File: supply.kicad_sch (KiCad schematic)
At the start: 39 parts, among them IC3 TPS259571DSGR, IC4 BQ27427YZFR, IC5 TPD6E001RSERG4, IC7 TPS62291DRVR, IC8 TPS62293DRVR, IC9 MP2722GRH-0000-Z, J4 UJ20-C-V-SMT-TR-68, J6 Conn_01x03

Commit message: cleaned up symbol fields table and removed unused or duplicate fields.
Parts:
- D1, D2: MFN (none) -> 755-SML-P12YTT86RR; MNR 755-SML-P12YTT86RR -> (none)
- IC3: MFN (none) -> 595-TPS259571DSGR; Manufacturer_Name Texas Instruments -> (none); Manufacturer_Part_Number TPS259571DSGR -> (none); Mouser Part Number 595-TPS259571DSGR -> (none); Mouser Price/Stock https://www.mouser.co.uk/ProductDetail/Texas-Instruments/TP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 -> (none)
- IC4: MFN (none) -> 595-BQ27427YZFR; Manufacturer_Name Texas Instruments -> (none); Manufacturer_Part_Number BQ27427YZFR -> (none); Mouser Part Number 595-BQ27427YZFR -> (none); Mouser Price/Stock https://www.mouser.co.uk/ProductDetail/Texas-Instruments/BQ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 -> (none)
- IC4: renamed from IC5; MFN (none) -> 595-TPD6E001RSERG4; Manufacturer_Name Texas Instruments -> (none); Manufacturer_Part_Number TPD6E001RSERG4 -> (none); Mouser Part Number 595-TPD6E001RSERG4 -> (none); Mouser Price/Stock https://www.mouser.co.uk/ProductDetail/Texas-Instruments/TP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 -> (none)
- IC5: renamed from IC9; MFN (none) -> 946-MP2722GRH-0000-Z; Manufacturer_Name Monolithic Power Systems (MPS) -> (none); Manufacturer_Part_Number MP2722GRH-0000-Z -> (none)
- IC6: renamed from IC7; MFN (none) -> 595-TPS62291DRVR; Manufacturer_Name Texas Instruments -> (none); Manufacturer_Part_Number TPS62291DRVR -> (none); Mouser Part Number 595-TPS62291DRVR -> (none); Mouser Price/Stock https://www.mouser.co.uk/ProductDetail/Texas-Instruments/TP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 -> (none)
- IC7: renamed from IC8; MFN (none) -> 595-TPS62293DRVR; Manufacturer_Name Texas Instruments -> (none); Manufacturer_Part_Number TPS62293DRVR -> (none); Mouser Part Number 595-TPS62293DRVR -> (none); Mouser Price/Stock https://www.mouser.co.uk/ProductDetail/Texas-Instruments/TP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 -> (none)
- J4: MFN (none) -> 179-UJ20-C-V-SMTTR68; Manufacturer_Name CUI Devices -> (none); Manufacturer_Part_Number UJ20-C-V-SMT-TR-68 -> (none); Mouser Part Number 179-UJ20-C-V-SMTTR68 -> (none); Mouser Price/Stock https://www.mouser.co.uk/ProductDetail/CUI-Devices/UJ20-C-V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 -> (none)
- renumbered C4 to C10, J6 to J5, L3 to L1, L1 to L2, L4 to L3, R16 to R10, R7 to R11, R10 to R12, R12 to R14, R18 to R15, R19 to R16, R8 to R7

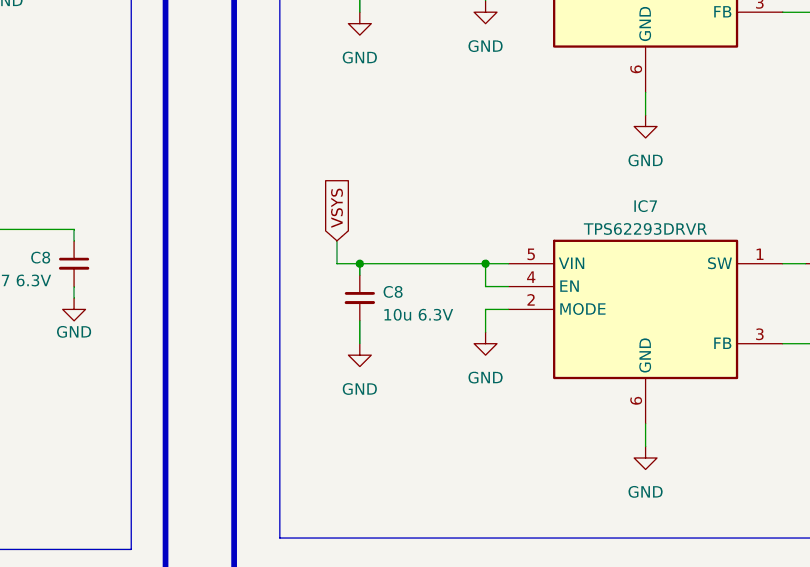
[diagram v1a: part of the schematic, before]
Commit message: switched to I2CB (so both M4 and A7 access), added 1v8 enable gpio and removed connection to vin
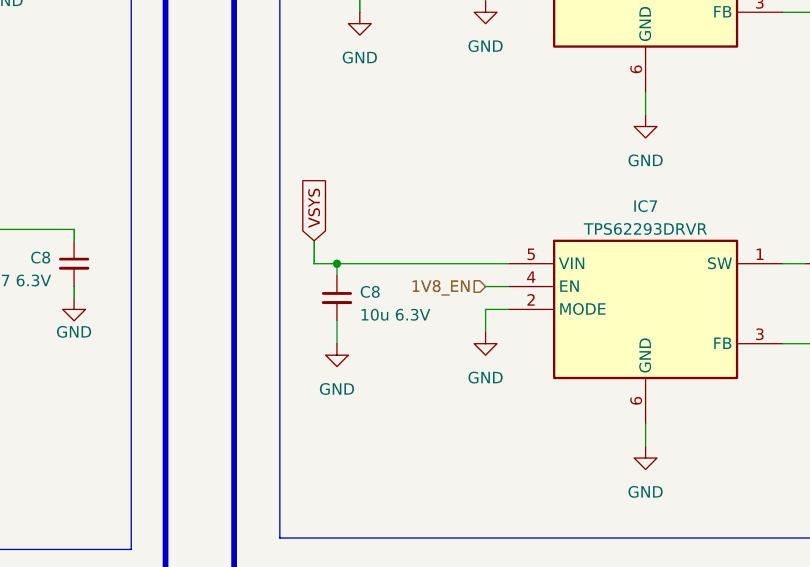
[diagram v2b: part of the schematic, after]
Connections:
- net VSYS: no longer IC7.4 (EN)
- new net 1V8_EN: IC7.4 (EN)
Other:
- moved on the sheet: C8
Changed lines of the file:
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@@
   (junction (at 254 134.62) (diameter 0) (color 0 0 0 0)
   )
-  (junction (at 330.2 176.53) (diameter 0) (color 0 0 0 0)
-  )
   (junction (at 240.03 45.72) (diameter 0) (color 0 0 0 0)
   )
@@
   (junction (at 238.76 134.62) (diameter 0) (color 0 0 0 0)
   )
-  (junction (at 316.23 176.53) (diameter 0) (color 0 0 0 0)
+  (junction (at 313.69 176.53) (diameter 0) (color 0 0 0 0)
   )
   (junction (at 261.62 134.62) (diameter 0) (color 0 0 0 0)
@@
     (stroke (width 0) (type default))
   )
-  (wire (pts (xy 316.23 182.88) (xy 316.23 185.42))
+  (wire (pts (xy 313.69 182.88) (xy 313.69 185.42))
     (stroke (width 0) (type default))
   )
@@
     (stroke (width 0) (type default))
   )
-  (wire (pts (xy 316.23 176.53) (xy 316.23 177.8))
+  (wire (pts (xy 313.69 176.53) (xy 313.69 177.8))
     (stroke (width 0) (type default))
   )
@@
     (stroke (width 0) (type default))
   )
-  (wire (pts (xy 330.2 176.53) (xy 332.74 176.53))
+  (wire (pts (xy 313.69 176.53) (xy 332.74 176.53))
     (stroke (width 0) (type default))
   )
@@
     (stroke (width 0) (type default))
   )
-  (wire (pts (xy 316.23 176.53) (xy 313.69 176.53))
+  (wire (pts (xy 313.69 176.53) (xy 311.15 176.53))
     (stroke (width 0) (type default))
   )
@@
     (stroke (width 0) (type default))
   )
-  (wire (pts (xy 330.2 176.53) (xy 330.2 179.07))
-    (stroke (width 0) (type default))
-  )
   (wire (pts (xy 266.7 223.52) (xy 269.24 223.52))
     (stroke (width 0) (type default))
@@
     (stroke (width 0) (type default))
   )
-  (wire (pts (xy 316.23 176.53) (xy 330.2 176.53))
-    (stroke (width 0) (type default))
-  )
   (wire (pts (xy 379.73 176.53) (xy 379.73 177.8))
     (stroke (width 0) (type default))
@@
     (stroke (width 0) (type default))
   )
-  (wire (pts (xy 313.69 173.99) (xy 313.69 176.53))
+  (wire (pts (xy 311.15 173.99) (xy 311.15 176.53))
     (stroke (width 0) (type default))
   )
@@
     )
   )
-  (global_label "VSYS" (shape input) (at 313.69 173.99 90) (fields_autoplaced)
+  (global_label "VSYS" (shape input) (at 311.15 173.99 90) (fields_autoplaced)
     (effects (font (size 1.27 1.27)) (justify left))
-    (property "Intersheetrefs" "${INTERSHEET_REFS}" (at 313.69 166.488 90)
+    (property "Intersheetrefs" "${INTERSHEET_REFS}" (at 311.15 166.488 90)
       (effects (font (size 1.27 1.27)) (justify left) hide)
     )
@@
       (effects (font (size 1.27 1.27)) (justify left) hide)
     )
+  )
+  (hierarchical_label "1V8_EN" (shape input) (at 330.2 179.07 180) (fields_autoplaced)
+    (effects (font (size 1.27 1.27)) (justify right))
   )
   (hierarchical_label "GASG_BIN" (shape input) (at 173.99 241.3 180) (fields_autoplaced)
@@
     )
   )
-  (symbol (lib_id "Device:C_Small") (at 316.23 180.34 0) (mirror y) (unit 1)
+  (symbol (lib_id "Device:C_Small") (at 313.69 180.34 0) (mirror y) (unit 1)
     (in_bom yes) (on_board yes) (dnp no)
-    (property "Reference" "C8" (at 318.77 179.7113 0)
-      (effects (font (size 1.27 1.27)) (justify right))
-    )
-    (property "Value" "10u 6.3V" (at 318.77 182.2513 0)
-      (effects (font (size 1.27 1.27)) (justify right))
-    )
-    (property "Footprint" "Capacitor_SMD:C_0402_1005Metric" (at 316.23 180.34 0)
-      (effects (font (size 1.27 1.27)) hide)
-    )
-    (property "Datasheet" "https://www.mouser.de/datasheet/2/281/1/GRM155R60J106ME05_01A-1983717.pdf" (at 316.23 180.34 0)
-      (effects (font (size 1.27 1.27)) hide)
-    )
-    (property "MFN" " 81-GRM155R60J106M05D " (at 316.23 180.34 0)
+    (property "Reference" "C8" (at 316.23 179.7113 0)
+      (effects (font (size 1.27 1.27)) (justify right))
+    )
+    (property "Value" "10u 6.3V" (at 316.23 182.2513 0)
+      (effects (font (size 1.27 1.27)) (justify right))
+    )
+    (property "Footprint" "Capacitor_SMD:C_0402_1005Metric" (at 313.69 180.34 0)
+      (effects (font (size 1.27 1.27)) hide)
+    )
+    (property "Datasheet" "https://www.mouser.de/datasheet/2/281/1/GRM155R60J106ME05_01A-1983717.pdf" (at 313.69 180.34 0)
+      (effects (font (size 1.27 1.27)) hide)
+    )
+    (property "MFN" " 81-GRM155R60J106M05D " (at 313.69 180.34 0)
       (effects (font (size 1.27 1.27)) hide)
     )
@@
     )
   )
-  (symbol (lib_id "power:GND") (at 316.23 185.42 0) (unit 1)
+  (symbol (lib_id "power:GND") (at 313.69 185.42 0) (unit 1)
     (in_bom yes) (on_board yes) (dnp no) (fields_autoplaced)
-    (property "Reference" "#PWR09" (at 316.23 191.77 0)
-      (effects (font (size 1.27 1.27)) hide)
-    )
-    (property "Value" "GND" (at 316.23 190.5 0)
-      (effects (font (size 1.27 1.27)))
-    )
-    (property "Footprint" "" (at 316.23 185.42 0)
-      (effects (font (size 1.27 1.27)) hide)
-    )
-    (property "Datasheet" "" (at 316.23 185.42 0)
-      (effects (font (size 1.27 1.27)) hide)
-    )
+    (property "Reference" "#PWR09" (at 313.69 191.77 0)
+      (effects (font (size 1.27 1.27)) hide)
+    )
+    (property "Value" "GND" (at 313.69 190.5 0)
+      (effects (font (size 1.27 1.27)))
+    )
+    (property "Footprint" "" (at 313.69 185.42 0)
+      (effects (font (size 1.27 1.27)) hide)
+    )
+    (property "Datasheet" "" (at 313.69 185.42 0)
+      (effects (font (size 1.27 1.27)) hide)
+    )

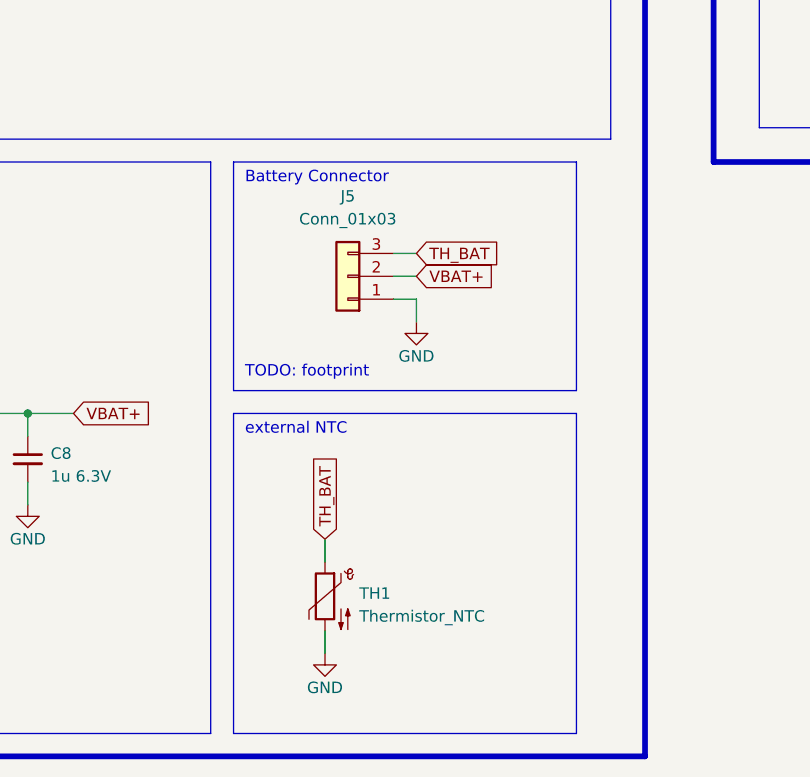
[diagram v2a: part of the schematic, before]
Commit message: Update battery connector in schematic
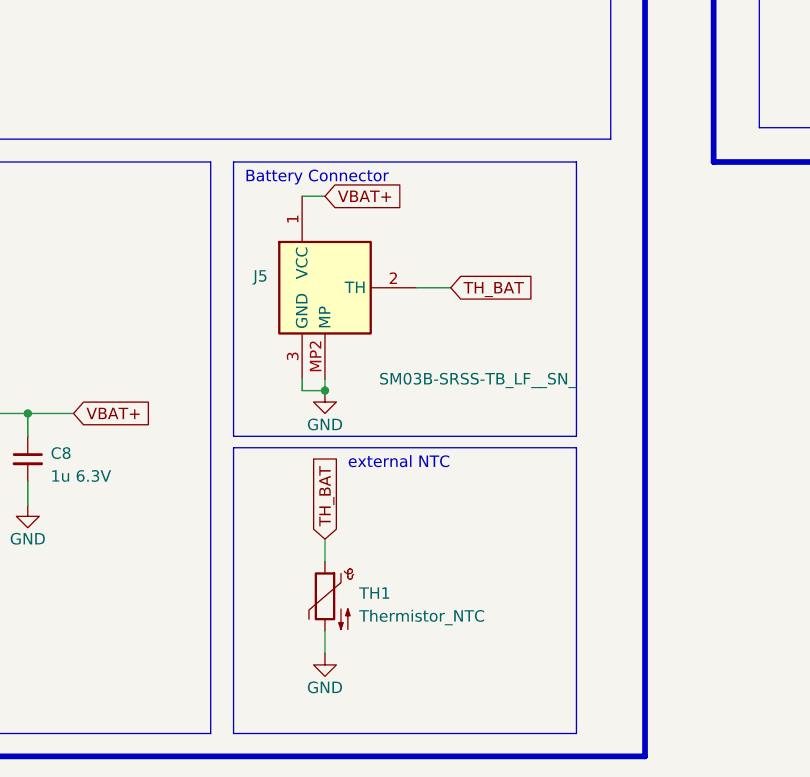
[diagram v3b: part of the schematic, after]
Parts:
- removed J5: Conn_01x03, symbol Connector_Generic:Conn_01x03
- added J5: SM03B-SRSS-TB_LF__SN_, SM03BSRSSTBLFSN, symbol ARMband:SM03B-SRSS-TB_LF__SN_
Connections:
- net EP: now also J5.3 (GND), J5.MP1 (MP), J5.MP2 (MP)
- net TH_BAT: now also J5.2 (TH)
- net VBAT+: now also J5.1 (VCC)
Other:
- note removed: "TODO: footprint"
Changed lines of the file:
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@@
   (junction (at 226.06 238.76) (diameter 0) (color 0 0 0 0)
+  )
+  (junction (at 259.08 236.22) (diameter 0) (color 0 0 0 0)
   )
   (junction (at 379.73 139.7) (diameter 0) (color 0 0 0 0)
@@
     (stroke (width 0) (type default))
   )
-  (polyline (pts (xy 287.02 238.76) (xy 287.02 274.32))
+  (polyline (pts (xy 287.02 242.57) (xy 287.02 274.32))
     (stroke (width 0) (type default))
   )
@@
     (stroke (width 0) (type default))
   )
+  (wire (pts (xy 259.08 234.95) (xy 259.08 236.22))
+    (stroke (width 0) (type default))
+  )
+  (wire (pts (xy 256.54 234.95) (xy 256.54 236.22))
+    (stroke (width 0) (type default))
+  )
   (wire (pts (xy 236.22 172.72) (xy 270.51 172.72))
     (stroke (width 0) (type default))
@@
     (stroke (width 0) (type default))
   )
-  (polyline (pts (xy 248.92 238.76) (xy 248.92 274.32))
+  (polyline (pts (xy 248.92 242.57) (xy 248.92 274.32))
     (stroke (width 0) (type default))
   )
@@
     (stroke (width 0) (type default))
   )
-  (polyline (pts (xy 248.92 210.82) (xy 248.92 236.22))
+  (polyline (pts (xy 248.92 210.82) (xy 248.92 241.3))
     (stroke (width 0) (type default))
   )
@@
     (stroke (width 0) (type default))
   )
-  (polyline (pts (xy 287.02 210.82) (xy 287.02 236.22))
+  (wire (pts (xy 256.54 214.63) (xy 259.08 214.63))
+    (stroke (width 0) (type default))
+  )
+  (polyline (pts (xy 287.02 210.82) (xy 287.02 241.3))
     (stroke (width 0) (type default))
   )
@@
     (stroke (width 0) (type default))
   )
-  (wire (pts (xy 266.7 223.52) (xy 269.24 223.52))
-    (stroke (width 0) (type default))
-  )
   (wire (pts (xy 182.88 53.34) (xy 182.88 55.88))
     (stroke (width 0) (type default))
@@
     (stroke (width 0) (type default))
   )
-  (wire (pts (xy 266.7 226.06) (xy 269.24 226.06))
+  (wire (pts (xy 269.24 224.79) (xy 273.05 224.79))
     (stroke (width 0) (type default))
   )
@@
     (stroke (width 0) (type default))
   )
+  (wire (pts (xy 256.54 236.22) (xy 259.08 236.22))
+    (stroke (width 0) (type default))
+  )
   (wire (pts (xy 228.6 35.56) (xy 232.41 35.56))
     (stroke (width 0) (type default))
@@
     (stroke (width 0) (type default))
   )
-  (wire (pts (xy 269.24 228.6) (xy 269.24 226.06))
-    (stroke (width 0) (type default))
-  )
   (wire (pts (xy 173.99 236.22) (xy 179.07 236.22))
     (stroke (width 0) (type default))
@@
     (stroke (width 0) (type default))
   )
-  (polyline (pts (xy 287.02 238.76) (xy 248.92 238.76))
+  (polyline (pts (xy 287.02 242.57) (xy 248.92 242.57))
     (stroke (width 0) (type default))
   )
@@
     (stroke (width 0) (type default))
   )
-  (polyline (pts (xy 248.92 236.22) (xy 287.02 236.22))
+  (polyline (pts (xy 248.92 241.3) (xy 287.02 241.3))
     (stroke (width 0) (type default))
   )
@@
   )
   (wire (pts (xy 370.84 176.53) (xy 373.38 176.53))
-    (stroke (width 0) (type default))
-  )
-  (wire (pts (xy 266.7 220.98) (xy 269.24 220.98))
     (stroke (width 0) (type default))
   )
@@
     (fill (type none))
   )
-  (text "TODO: footprint" (at 250.19 234.95 0)
-    (effects (font (size 1.27 1.27)) (justify left bottom))
-  )
   (text "Same value\nas NTC@25°C" (at 184.15 167.64 0)
     (effects (font (size 1.27 1.27)) (justify left bottom))
@@
     (effects (font (size 1.27 1.27)) (justify left bottom))
   )
-  (text "external NTC" (at 250.19 241.3 0)
+  (text "external NTC" (at 261.62 245.11 0)
     (effects (font (size 1.27 1.27)) (justify left bottom))
   )
@@
     )
   )
-  (global_label "VBAT+" (shape input) (at 269.24 223.52 0) (fields_autoplaced)
+  (global_label "VBAT+" (shape input) (at 259.08 214.63 0) (fields_autoplaced)
     (effects (font (size 1.27 1.27)) (justify left))
-    (property "Intersheetrefs" "${INTERSHEET_REFS}" (at 278.133 223.52 0)
+    (property "Intersheetrefs" "${INTERSHEET_REFS}" (at 267.973 214.63 0)
       (effects (font (size 1.27 1.27)) (justify left) hide)
     )
@@
     )
   )
-  (global_label "TH_BAT" (shape input) (at 269.24 220.98 0) (fields_autoplaced)
+  (global_label "TH_BAT" (shape input) (at 273.05 224.79 0) (fields_autoplaced)
     (effects (font (size 1.27 1.27)) (justify left))
-    (property "Intersheetrefs" "${INTERSHEET_REFS}" (at 278.8171 220.98 0)
+    (property "Intersheetrefs" "${INTERSHEET_REFS}" (at 282.6271 224.79 0)
       (effects (font (size 1.27 1.27)) (justify left) hide)
     )
@@
     )
   )
-  (symbol (lib_id "power:GND") (at 269.24 228.6 0) (unit 1)
-    (in_bom yes) (on_board yes) (dnp no)
-    (property "Reference" "#PWR021" (at 269.24 234.95 0)
-      (effects (font (size 1.27 1.27)) hide)
-    )
-    (property "Value" "GND" (at 269.24 232.41 0)
-      (effects (font (size 1.27 1.27)))
-    )
-    (property "Footprint" "" (at 269.24 228.6 0)
-      (effects (font (size 1.27 1.27)) hide)
-    )
-    (property "Datasheet" "" (at 269.24 228.6 0)
+  (symbol (lib_id "power:GND") (at 259.08 236.22 0) (mirror y) (unit 1)
+    (in_bom yes) (on_board yes) (dnp no)
+    (property "Reference" "#PWR021" (at 259.08 242.57 0)
+      (effects (font (size 1.27 1.27)) hide)
+    )
+    (property "Value" "GND" (at 259.08 240.03 0)
+      (effects (font (size 1.27 1.27)))
+    )
+    (property "Footprint" "" (at 259.08 236.22 0)
+      (effects (font (size 1.27 1.27)) hide)
+    )
+    (property "Datasheet" "" (at 259.08 236.22 0)
       (effects (font (size 1.27 1.27)) hide)
     )
@@
         (path "/017c50c6-333c-4d31-ad5a-278994a09b14/ae5dc462-dca9-40e4-ba02-6b87a86a4904"
           (reference "#PWR040") (unit 1)
-        )
-      )
-    )
-  )
-  (symbol (lib_id "Connector_Generic:Conn_01x03") (at 261.62 223.52 180) (unit 1)
-    (in_bom yes) (on_board yes) (dnp no) (fields_autoplaced)
-    (property "Reference" "J5" (at 261.62 214.63 0)
-      (effects (font (size 1.27 1.27)))
-    )
-    (property "Value" "Conn_01x03" (at 261.62 217.17 0)
-      (effects (font (size 1.27 1.27)))
-    )
-    (property "Footprint" "" (at 261.62 223.52 0)
-      (effects (font (size 1.27 1.27)) hide)
-    )
-    (property "Datasheet" "~" (at 261.62 223.52 0)
-      (effects (font (size 1.27 1.27)) hide)
-    )
-    (pin "1")
-    (pin "2")
-    (pin "3")
-    (instances
-      (project "armband"
-        (path "/017c50c6-333c-4d31-ad5a-278994a09b14/ae5dc462-dca9-40e4-ba02-6b87a86a4904"
-          (reference "J5") (unit 1)
         )
       )
@@
         )
       )
+    )
+  )
+  (symbol (lib_id "ARMband:SM03B-SRSS-TB_LF__SN_") (at 248.92 222.25 0) (unit 1)
+    (in_bom yes) (on_board yes) (dnp no)
+    (property "Reference" "J5" (at 252.73 223.52 0)
+      (effects (font (size 1.27 1.27)) (justify right))
+    )
+    (property "Value" "SM03B-SRSS-TB_LF__SN_" (at 287.02 234.95 0)
+      (effects (font (size 1.27 1.27)) (justify right))
+    )
+    (property "Footprint" "SM03BSRSSTBLFSN" (at 267.97 317.17 0)
+      (effects (font (size 1.27 1.27)) (justify left top) hide)
+    )
+    (property "Datasheet" "http://www.jst-mfg.com/product/pdf/eng/eSR.pdf" (at 267.97 417.17 0)
+      (effects (font (size 1.27 1.27)) (justify left top) hide)
+    )
+    (property "Height" "2.9" (at 267.97 617.17 0)
+      (effects (font (size 1.27 1.27)) (justify left top) hide)
+    )
+    (property "Manufacturer_Name" "JST (JAPAN SOLDERLESS TERMINALS)" (at 267.97 717.17 0)
+      (effects (font (size 1.27 1.27)) (justify left top) hide)
+    )
+    (property "Manufacturer_Part_Number" "SM03B-SRSS-TB(LF)(SN)" (at 267.97 817.17 0)
+      (effects (font (size 1.27 1.27)) (justify left top) hide)
+    )
+    (property "Mouser Part Number" "" (at 267.97 917.17 0)
+      (effects (font (size 1.27 1.27)) (justify left top) hide)
+    )
+    (property "Mouser Price/Stock" "" (at 267.97 1017.17 0)
+      (effects (font (size 1.27 1.27)) (justify left top) hide)
+    )
+    (property "Arrow Part Number" "SM03B-SRSS-TB(LF)(SN)" (at 267.97 1117.17 0)
+      (effects (font (size 1.27 1.27)) (justify left top) hide)
+    )
+    (property "Arrow Price/Stock" "https://www.arrow.com/en/products/sm03b-srss-tb-lf-sn/jst-manufacturing?region=europe" (at 267.97 1217.17 0)
+      (effects (font (size 1.27 1.27)) (justify left top) hide)
+    )
+    (pin "3")
+    (pin "2")
+    (pin "1")
+    (pin "MP1")
+    (pin "MP2")
+    (instances
+      (project "armband"
+        (path "/017c50c6-333c-4d31-ad5a-278994a09b14/ae5dc462-dca9-40e4-ba02-6b87a86a4904"
+          (reference "J5") (unit 1)
+        )
+      )
